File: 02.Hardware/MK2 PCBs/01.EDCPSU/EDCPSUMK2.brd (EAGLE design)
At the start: 96 x 60.8 mm, 182 parts, among them IC1 IP2721, J1 DX07S016JA1R1500, J3 AVR_ISP, J4 FTDI_DEVICE, J6 Display, K1 FLEX8, Q2 2N7002PW, Q4 2N7002PW, Q5 2N7002PW, Q9 2N7002PW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

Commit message: Revision de version definitva Javi
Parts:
- R47, R48: value (none) -> 100R
- R49: value (none) -> 10k
- R50: value (none) -> 56k
- R51: value (none) -> 220k
- R55, R56: value (none) -> 5k1
- R59: value (none) -> 1k
- R62: value (none) -> 100k
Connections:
- net GND_IN: now also J1.S1, J1.S2, J1.S3, J1.S4, J1.S5, J1.S6
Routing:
- net VCC-ISO: track 143.5 -> 141.0 mm
- net VOUT: track 45.7 -> 47.7 mm
- net GND: track 188.0 -> 189.8 mm
- net SAFETY_EN_DCDC: track 54.9 -> 53.9 mm

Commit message: Update Note 22-RTR (Ready To Revision)
Add Resistor N.A for Divisor
Connect USb Shield to GND
Fix silkcreen and Position
Fix IN_OVC to MCPU
Plane for VOUT and GND in Flex Connection
Fix Test Pint Positions
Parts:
- removed GND, PEDAL+, PEDAL-, VOUT+: TEST-POINT3, SparkFun-Connectors:PAD.03X.03
- removed TP13: (no value), SparkFun-Connectors:1X01_POGOPIN_HOLE_LARGE
- added R34: N.A, SparkFun-Resistors:0603
- moved TP12 17.9 mm to (35.8, 35.1)
- moved TP3 15.7 mm to (50.9, 44.2)
- moved D8 5.45 mm to (29.3, 46.3)
- moved TP11 2.06 mm to (35.7, 32.5)
- moved R59 0.22 mm to (31.5, 27.3)
- moved R56 0.15 mm to (21.9, 24.5)
- renumbered IC1 to U10
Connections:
- removed net TEST: TP13.1
- removed net VOUT+: TP11.1
- net GND: no longer GND.P$1
- net GND_IN: now also R34.1
- net IN_OVC: no longer U1.13
- net N$59: now also R34.2
- net PEDAL+: no longer PEDAL+.P$1
- net PEDAL-: no longer PEDAL-.P$1
- net VOUT: now also TP11.1; no longer VOUT+.P$1
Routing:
- net GND_IN: track 18.1 -> 37.6 mm, vias 10 -> 11
- net IN_OVC: track 143.3 -> 160.0 mm, vias 4 -> 3
- net GND: track 189.8 -> 205.6 mm, vias 150 -> 154
- net VOUT: track 47.7 -> 60.3 mm, vias 2 -> 5
- net IN+: track 27.5 -> 31.3 mm
- net N$59: track 7.03 -> 10.2 mm
- net VCC: track 70.6 -> 73.3 mm
- net SPARE: track 73.4 -> 75.4 mm
- net VOSEN: track 88.9 -> 87.3 mm
- net VCC-ISO: track 141.0 -> 139.6 mm
- added copper zone on layer 1, net VOUT
- added copper zone on layer 16, net VOUT
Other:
- board text removed: "0V"
- board text removed: "C"
- board text removed: "TEST"
- board text removed: "VO+"
- board text removed: "VO-"

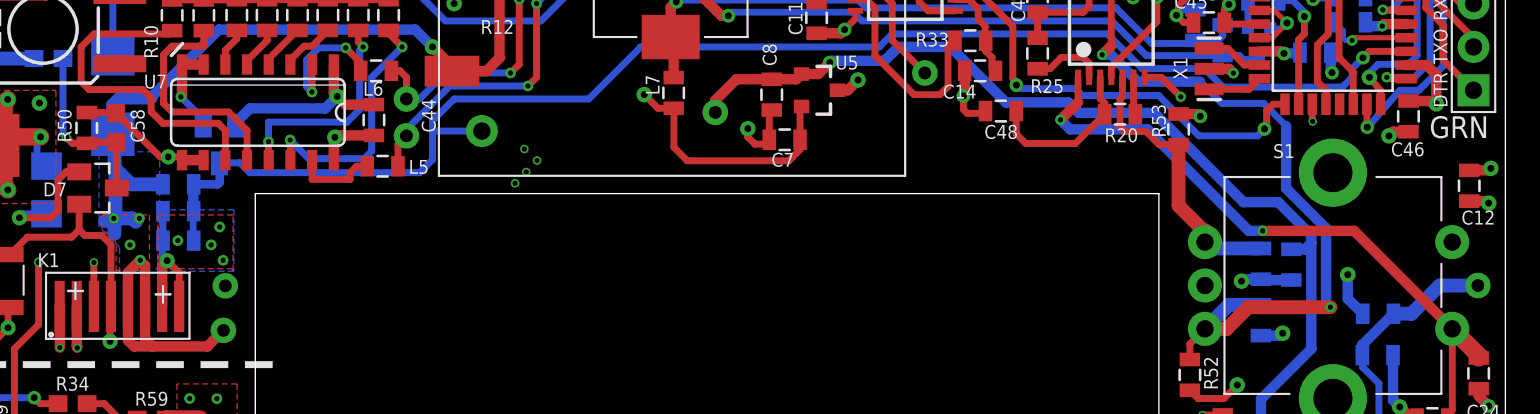
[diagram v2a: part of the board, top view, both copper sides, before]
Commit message: Añadido SPARE2 + revisión
Se añade SPARE2 con R y Pad para  tener un punto de acceso al pin 13 de CPU.
Pequeños cambios en revisión
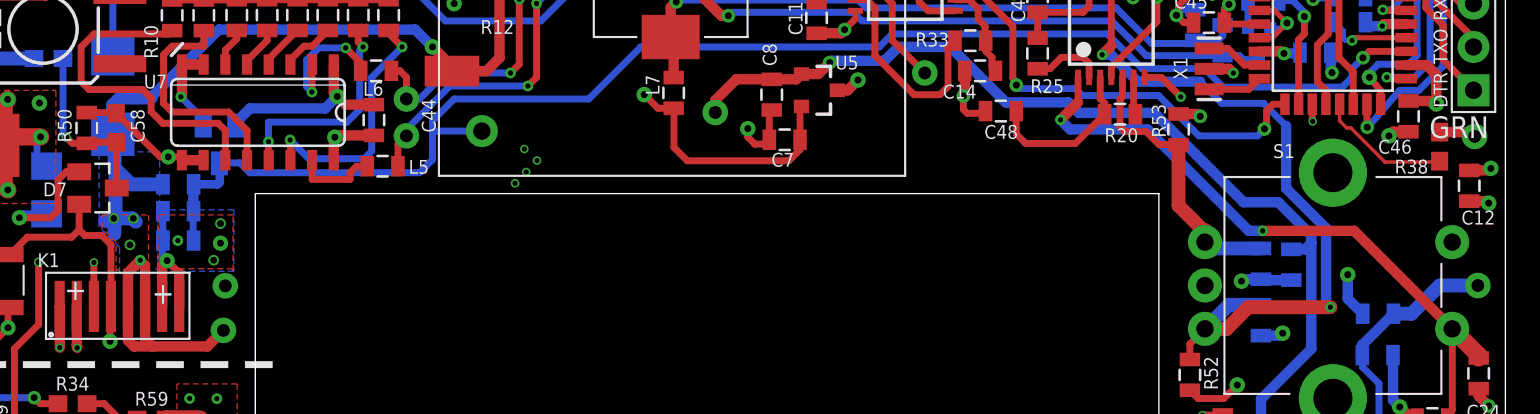
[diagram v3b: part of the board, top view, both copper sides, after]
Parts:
- added R38: N.A, SparkFun-Resistors:0603
- added TP1: (no value), SparkFun-Connectors:1X01_POGOPIN_HOLE_LARGE
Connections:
- new net N$38: R38.2, TP1.1
- new net SPARE2: R38.1, U1.13
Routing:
- net SPARE2: track 0.00 -> 7.85 mm
- net N$38: track 0.00 -> 2.15 mm
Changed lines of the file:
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@@
 <drawing>
 <settings>
-<setting alwaysvectorfont="yes"/>
+<setting alwaysvectorfont="no"/>
 <setting keepoldvectorfont="yes"/>
 <setting verticaltext="up"/>
@@
 <layer number="39" name="tKeepout" color="4" fill="11" visible="yes" active="yes"/>
 <layer number="40" name="bKeepout" color="1" fill="11" visible="yes" active="yes"/>
-<layer number="41" name="tRestrict" color="4" fill="10" visible="yes" active="yes"/>
+<layer number="41" name="tRestrict" color="4" fill="10" visible="no" active="yes"/>
 <layer number="42" name="bRestrict" color="1" fill="10" visible="yes" active="yes"/>
 <layer number="43" name="vRestrict" color="2" fill="10" visible="no" active="yes"/>
@@
 </element>
 <element name="C46" library="SparkFun" package="0805" value="100n" x="105.124" y="45.024" smashed="yes" rot="R90">
-<attribute name="NAME" x="106.0762" y="43.4985" size="0.8128" layer="25" font="vector" rot="R180"/>
+<attribute name="NAME" x="105.3262" y="43.6485" size="0.8128" layer="25" font="vector" rot="R180"/>
 <attribute name="VALUE" x="106.521" y="44.008" size="0.4064" layer="27" rot="R90"/>
 </element>
@@
 <attribute name="VALUE" x="26.9" y="27.438" size="0.6096" layer="27" font="vector" ratio="20" align="top-center"/>
 </element>
+<element name="TP1" library="SparkFun-Connectors" package="1X01_POGOPIN_HOLE_LARGE" value="" x="109" y="43.85" smashed="yes"/>
+<element name="R38" library="SparkFun-Resistors" library_urn="urn:adsk.eagle:library:532" package="0603" package3d_urn="urn:adsk.eagle:package:39650/1" value="N.A" x="106.95" y="43.25" smashed="yes" rot="R90">
+<attribute name="NAME" x="105.3" y="42.488" size="0.8128" layer="25" font="vector" rot="R180" align="bottom-center"/>
+<attribute name="PROD_ID" value=" " x="106.95" y="43.25" size="1.778" layer="27" rot="R90" display="off"/>
+<attribute name="VALUE" x="107.712" y="43.25" size="0.6096" layer="27" font="vector" ratio="20" rot="R90" align="top-center"/>
+</element>
 </elements>
 <signals>
@@
 <wire x1="32.1604" y1="37.801" x2="32.1604" y2="36.8496" width="0.4064" layer="16"/>
 <wire x1="32.435" y1="36.575" x2="33.145" y2="35.865" width="0.4064" layer="1"/>
-<wire x1="33.145" y1="35.865" x2="33.145" y2="33.895" width="0.4064" layer="1"/>
+<wire x1="33.145" y1="35.865" x2="33.145" y2="33.895" width="0.6096" layer="1"/>
 <wire x1="32.1896" y1="37.749" x2="32.1896" y2="39.471" width="0.4064" layer="16"/>
 <wire x1="34.5501" y1="44.4741" x2="34.5501" y2="44.8589" width="0.4064" layer="16"/>
@@
 <wire x1="27.4892" y1="53.7108" x2="23.844" y2="53.7108" width="0.4064" layer="16"/>
 <wire x1="29.2579" y1="51.9421" x2="27.4892" y2="53.7108" width="0.4064" layer="16"/>
-<polygon width="0.4064" layer="1" isolate="0.254" rank="2">
+<polygon width="0.1016" layer="1" isolate="0.254" rank="2">
 <vertex x="31.9" y="39.25"/>
 <vertex x="31.9" y="36.2"/>
@@
 <vertex x="36.3" y="39.25"/>
 </polygon>
-<via x="35.512" y="38.547" extent="1-16" drill="0.3048" diameter="0.635"/>
+<via x="35.562" y="38.747" extent="1-16" drill="0.4" diameter="0.635"/>
 <via x="33.062" y="37.747" extent="1-16" drill="0.3048" diameter="0.635"/>
-<via x="35.012" y="37.497" extent="1-16" drill="0.3048" diameter="0.635"/>
-<via x="35.712" y="36.597" extent="1-16" drill="0.3048" diameter="0.635"/>
+<via x="35.562" y="37.597" extent="1-16" drill="0.4" diameter="0.9"/>
+<via x="35.162" y="36.597" extent="1-16" drill="0.4" diameter="0.635"/>
 <polygon width="0.1524" layer="16" isolate="0.4064" rank="2">
 <vertex x="32.05" y="39.55"/>
@@
 <wire x1="30.145" y1="35.88" x2="30.862" y2="36.597" width="0.6096" layer="1"/>
 <contactref element="TP11" pad="1"/>
-<polygon width="0.4064" layer="1" isolate="0.254">
-<vertex x="31.4" y="36"/>
-<vertex x="29.5" y="36"/>
+<polygon width="0.1016" layer="1" isolate="0.254">
+<vertex x="31.35" y="36.05"/>
+<vertex x="29.55" y="36.05"/>
 <vertex x="29.45" y="35.95"/>
 <vertex x="29.45" y="37.65"/>
@@
 <vertex x="28.6" y="39.2"/>
 <vertex x="28.65" y="39.25"/>
-<vertex x="31.4" y="39.25"/>
+<vertex x="31.35" y="39.25"/>
 </polygon>
-<via x="30.262" y="37.497" extent="1-16" drill="0.3048" diameter="0.635"/>
-<via x="29.312" y="39.047" extent="1-16" drill="0.3048" diameter="0.635"/>
+<via x="30.262" y="37.497" extent="1-16" drill="0.4" diameter="0.635"/>
+<via x="29.312" y="39.047" extent="1-16" drill="0.4" diameter="0.635"/>
 <wire x1="31.4896" y1="46.1236" x2="29.7236" y2="46.1236" width="0.8128" layer="16"/>
 <wire x1="29.2579" y1="45.6579" x2="29.2579" y2="43.9775" width="0.8128" layer="16"/>
@@
 <wire x1="29.312" y1="39.047" x2="29.16530625" y2="38.9" width="0.8128" layer="16"/>
 <wire x1="29.16530625" y1="38.9" x2="28.8" y2="38.9" width="0.8128" layer="16"/>
-<via x="30.812" y="39.047" extent="1-16" drill="0.3048" diameter="0.635"/>
+<via x="30.462" y="39.047" extent="1-16" drill="0.4" diameter="0.635"/>
 <wire x1="35.734" y1="32.492" x2="34.792" y2="31.55" width="0.6096" layer="1"/>
 <wire x1="31.145" y1="32.005" x2="31.145" y2="33.895" width="0.6096" layer="1"/>
@@
 <wire x1="79.412" y1="54.452" x2="79.805" y2="54.845" width="0.4064" layer="1"/>
 </signal>
+<signal name="SPARE2">
+<contactref element="U1" pad="13"/>
+<wire x1="101.0917" y1="45.7352" x2="101.0917" y2="44.7583" width="0.2032" layer="1"/>
+<wire x1="101.0917" y1="44.7583" x2="101.5" y2="44.35" width="0.2032" layer="1"/>
+<wire x1="101.74420625" y1="44.35" x2="101.5" y2="44.35" width="0.2032" layer="1"/>
+<wire x1="101.74420625" y1="44.35" x2="103.74420625" y2="42.35" width="0.2032" layer="1"/>
+<contactref element="R38" pad="1"/>
+<wire x1="106.9" y1="42.35" x2="106.95" y2="42.4" width="0.2032" layer="1"/>
+<wire x1="103.74420625" y1="42.35" x2="106.9" y2="42.35" width="0.2032" layer="1"/>
+</signal>
+<signal name="N$38">
+<contactref element="TP1" pad="1"/>
+<contactref element="R38" pad="2"/>
+<wire x1="109" y1="43.85" x2="108.6" y2="43.85" width="0.6096" layer="1"/>
+<wire x1="108.6" y1="43.85" x2="108.35" y2="44.1" width="0.6096" layer="1"/>
+<wire x1="108.35" y1="44.1" x2="106.95" y2="44.1" width="0.6096" layer="1"/>
+</signal>
 </signals>

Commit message: Pequeños cambios ruteado
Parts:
- moved C17 0.27 mm to (18.1, 59.2)
- moved C18 0.16 mm to (21.3, 59.3)
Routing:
- net VO_TPS: track 43.9 -> 45.1 mm, vias 3 -> 5
- net GND: track 205.6 -> 204.7 mm
- net VOUT: track 60.3 -> 59.8 mm, vias 5 -> 7
- added copper zone on layer 1, net VO_TPS
- added copper zone on layer 16, net VO_TPS
